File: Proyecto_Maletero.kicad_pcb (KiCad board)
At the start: 2 copper layers, 44 parts, among them J1 DE9_Pins, J2 Conn_01x02, J3 Conn_01x02, J4 Conn_01x03, J5 Conn_01x02, J6 DE9_Pins, J8 Conn_01x02, J9 Conn_01x02, K1 FINDER-34.51, Q2 MMBT5550L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

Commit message: Layout inicio
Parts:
- removed C17: 100n, Capacitor_SMD:C_0805_2012Metric
- J8, J9: footprint TerminalBlock_Phoenix:TerminalBlock_Phoenix_MKDS-1,5-3-5.08_1x03_P5.08mm_Horizontal -> TerminalBlock_Phoenix:TerminalBlock_Phoenix_MKDS-1,5-2_1x02_P5.00mm_Horizontal
- moved R7 76.9 mm to (131.0, 54.3), turned to -90 degrees
- moved R6 71.8 mm to (125.7, 50.0)
- moved C13 56.4 mm to (117.8, 54.0), turned to -90 degrees
- moved U2 53.6 mm to (123.9, 54.3)
- moved C14 49.9 mm to (115.0, 70.4), turned to 90 degrees
- moved J6 47.2 mm to (128.6, 35.0), turned to -90 degrees
- moved C8 45.9 mm to (105.5, 38.6), turned to 180 degrees
- moved C18 43.0 mm to (80.2, 24.8), turned to 180 degrees
- moved C15 42.8 mm to (96.2, 25.0)
- moved C3 41.7 mm to (100.6, 56.6)
- moved R2 41.1 mm to (95.0, 49.5), turned to -90 degrees
- moved C4 40.5 mm to (95.5, 45.5), turned to -90 degrees
- moved K1 39.3 mm to (106.5, 42.2)
- moved C5 38.4 mm to (91.5, 45.5), turned to -90 degrees
- moved R1 37.9 mm to (92.2, 49.4), turned to 90 degrees
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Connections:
- C7 pad 1: Osc_1 -> Osc_2
- C9 pad 1: GND -> VRth
- C9 pad 2: VCC -> GND
- J3 pad 1: VBAT -> VBATERIA
- U7 pad 5: unconnected-(U7-VM-Pad5) -> VBAT
- Y1 pad 1: Osc_1 -> Osc_2
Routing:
- net VCC: track 0.00 -> 138.6 mm
- net VBAT: track 0.00 -> 51.4 mm
- net GND: track 0.00 -> 18.1 mm, vias 0 -> 21
- net SENSE: track 0.00 -> 16.2 mm
- net VBATERIA: track 0.00 -> 13.3 mm
- net Net-(D2-A): track 0.00 -> 10.2 mm
- net VRth: track 0.00 -> 6.35 mm
- net Net-(Q2-B): track 0.00 -> 5.67 mm
- net Vopam: track 0.00 -> 5.37 mm
- added copper zone on B.Cu, net GND

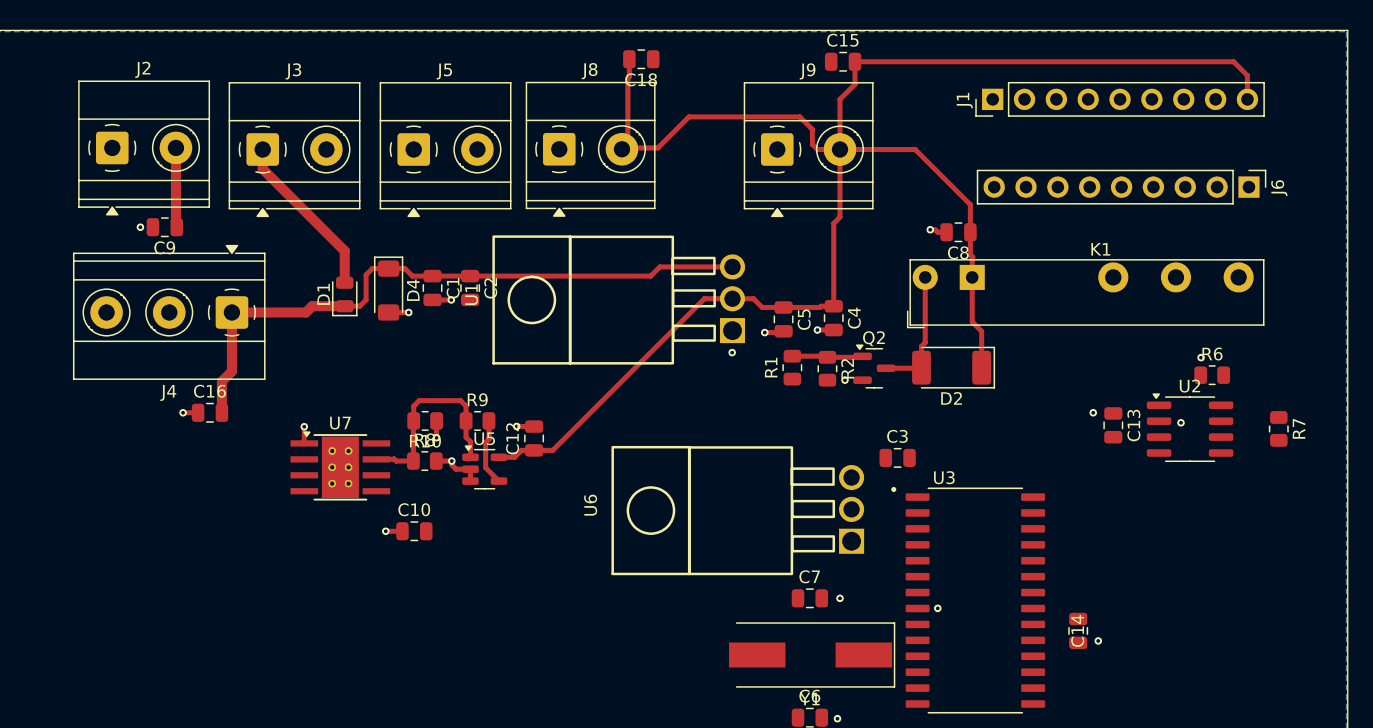
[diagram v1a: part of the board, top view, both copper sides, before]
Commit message: Capas y DE-9
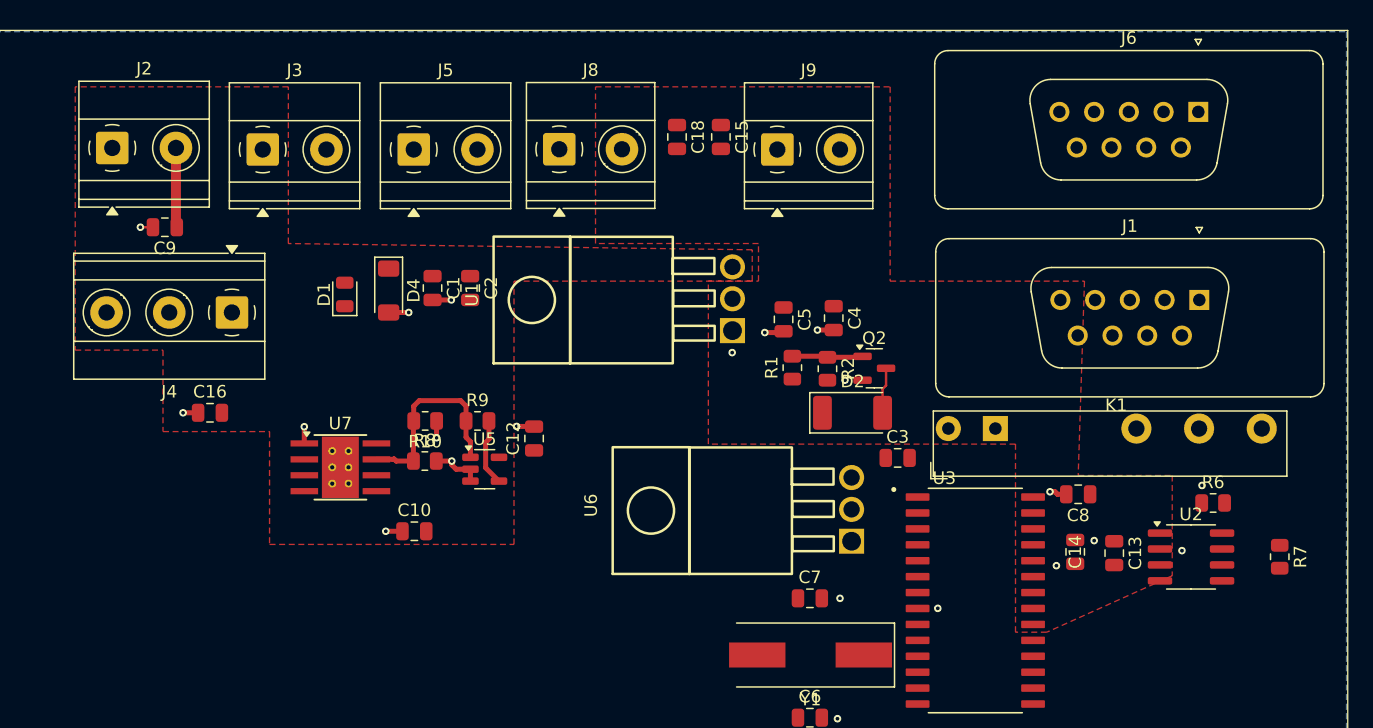
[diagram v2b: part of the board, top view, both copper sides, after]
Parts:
- J1, J6: footprint Connector_PinHeader_2.54mm:PinHeader_1x09_P2.54mm_Vertical -> Connector_Dsub:DSUB-9_Socket_Vertical_P2.77x2.84mm
- moved C8 23.0 mm to (115.0, 59.5)
- moved J1 23.0 mm to (124.7, 44.0), turned to 0 degrees
- moved K1 12.2 mm to (108.4, 54.3)
- moved C15 11.4 mm to (86.5, 31.0), turned to -90 degrees
- moved R6 10.2 mm to (125.8, 60.2)
- moved R7 10.2 mm to (131.1, 64.5)
- moved U2 10.2 mm to (124.0, 64.5)
- moved C13 10.2 mm to (117.9, 64.2)
- moved D2 8.68 mm to (97.0, 53.0), turned to 0 degrees
- moved J6 7.23 mm to (124.6, 29.0), turned to 0 degrees
- moved C18 6.82 mm to (83.0, 31.0), turned to -90 degrees
- moved C14 6.31 mm to (114.8, 64.1)
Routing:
- net VCC: track 138.6 -> 0.00 mm
- net VBAT: track 51.4 -> 0.00 mm
- net VBATERIA: track 13.3 -> 0.00 mm
- net Net-(D2-A): track 10.2 -> 3.66 mm
- net GND: track 18.1 -> 19.1 mm
- added copper zone on F.Cu, net VBAT
- added copper zone on F.Cu, net VCC

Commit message: Actulizacion layout
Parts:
- J1, J6: footprint Connector_Dsub:DSUB-9_Socket_Vertical_P2.77x2.84mm -> Connector_Dsub:DSUB-9_Pins_Horizontal_P2.77x2.84mm_EdgePinOffset4.94mm_Housed_MountingHolesOffset4.94mm
- moved J6 97.6 mm to (38.0, 74.1)
- moved C8 78.5 mm to (36.5, 59.2), turned to -90 degrees
- moved K1 78.1 mm to (30.5, 60.2), turned to 90 degrees
- moved R7 53.0 mm to (78.4, 59.4), turned to 0 degrees
- moved D2 47.3 mm to (49.7, 53.0), turned to -90 degrees
- moved Q2 45.8 mm to (53.2, 54.7), turned to -90 degrees
- moved C3 44.7 mm to (56.0, 54.4), turned to 90 degrees
- moved R6 43.1 mm to (82.7, 63.1)
- moved U2 42.9 mm to (81.2, 67.2)
- moved C6 42.5 mm to (54.4, 61.0), turned to 180 degrees
- moved R2 41.8 mm to (53.2, 51.0), turned to 180 degrees
- moved J1 41.2 mm to (94.1, 71.6), turned to 90 degrees
- moved Y1 39.8 mm to (54.3, 66.0), turned to 0 degrees
- moved C14 39.4 mm to (76.4, 73.2)
- moved C7 39.3 mm to (54.4, 70.5), turned to 180 degrees
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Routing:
- net Sensor_Pie: track 0.00 -> 16.4 mm
- net VCC: track 0.00 -> 14.1 mm
- net VRth: track 6.35 -> 0.09 mm
- net GND: track 19.1 -> 24.5 mm, vias 21 -> 19
- net Net-(D2-A): track 3.66 -> 0.00 mm
- net VBAT: track 0.00 -> 2.76 mm
- removed copper zone on F.Cu, net VBAT
- removed copper zone on F.Cu, net VCC
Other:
- board outline added: 74.8 x 59.6 mm

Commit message: Layout final v.1
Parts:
- added REF**: MountingHole_2.5mm, MountingHole:MountingHole_2.5mm, F.Cu at (95.8, 76.8)
- added REF**: MountingHole_2.5mm, MountingHole:MountingHole_2.5mm, F.Cu at (29.9, 28.6)
- added REF**: MountingHole_2.5mm, MountingHole:MountingHole_2.5mm, F.Cu at (31.6, 78.1)
- added REF**: MountingHole_2.5mm, MountingHole:MountingHole_2.5mm, F.Cu at (98.8, 27.4)
- J1, J6: footprint Connector_Dsub:DSUB-9_Pins_Horizontal_P2.77x2.84mm_EdgePinOffset4.94mm_Housed_MountingHolesOffset4.94mm -> Connector_Dsub:DSUB-9_Pins_Horizontal_P2.77x2.54mm_EdgePinOffset9.40mm
- moved J6 38.3 mm to (76.1, 70.0)
- moved C3 35.9 mm to (36.8, 24.1), turned to 0 degrees
- moved C6 17.0 mm to (38.5, 67.0)
- moved C7 16.8 mm to (38.3, 75.4)
- moved C9 13.4 mm to (64.9, 23.8), turned to 0 degrees
- moved C14 13.4 mm to (63.4, 69.8)
- moved U3 12.6 mm to (55.6, 68.9)
- moved Y1 11.9 mm to (43.5, 70.8), turned to 90 degrees
- moved C16 8.45 mm to (50.9, 37.3), turned to 180 degrees
- moved R1 7.84 mm to (49.7, 55.2), turned to 180 degrees
- moved D2 6.65 mm to (55.8, 50.3), turned to 90 degrees
- moved Q2 6.33 mm to (49.7, 49.5), turned to 90 degrees
- moved R7 6.26 mm to (82.5, 64.1), turned to -90 degrees
- moved C13 5.51 mm to (77.2, 67.3)
- moved U2 5.51 mm to (77.3, 63.3)
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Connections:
- C1 pad 2: GND -> GNDPWR
- C10 pad 1: GND -> GNDPWR
- C12 pad 2: GND -> GNDPWR
- C15 pad 1: GND -> GNDPWR
- C16 pad 1: GND -> GNDPWR
- C18 pad 1: GND -> GNDPWR
- C2 pad 2: GND -> GNDPWR
- C3 pad 2: GND -> GNDPWR
- C4 pad 2: GND -> GNDPWR
- C5 pad 2: GND -> GNDPWR
- C8 pad 2: GND -> GNDPWR
- C9 pad 2: GND -> GNDPWR
- D4 pad 2: GND -> GNDPWR
- J2 pad 1: GND -> GNDPWR
- J3 pad 2: GND -> GNDPWR
- J4 pad 2: GND -> GNDPWR
- Q2 pad 2: GND -> GNDPWR
- R10 pad 1: GND -> GNDPWR
- R2 pad 2: GND -> GNDPWR
- R8 pad 2: GND -> GNDPWR
- U1 pad 1: GND -> GNDPWR
- U5 pad 2: GND -> GNDPWR
- U5 pad 3: GND -> GNDPWR
- U6 pad 1: GND -> unconnected-(U6-GND-Pad1)
- U7 pad 1: GND -> GNDPWR
- U7 pad 9: GND -> GNDPWR
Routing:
- net VCC: track 14.1 -> 180.6 mm, vias 0 -> 1
- net VBAT: track 2.76 -> 97.4 mm, vias 0 -> 2
- net SENAL_RELE: track 0.00 -> 65.8 mm
- net Manual_Close: track 0.00 -> 64.6 mm, vias 0 -> 2
- net Sensor_Pie: track 16.4 -> 75.6 mm
- net VRth: track 0.09 -> 53.8 mm
- net Vopam: track 5.37 -> 41.0 mm, vias 0 -> 2
- net Net-(D2-A): track 0.00 -> 34.1 mm
- net Motor+: track 0.00 -> 28.9 mm, vias 0 -> 2
- net Motor-: track 0.00 -> 28.2 mm, vias 0 -> 2
- net PH_B: track 0.00 -> 25.4 mm
- net INPUT_RELE: track 0.00 -> 25.1 mm
- net GNDPWR: track 0.00 -> 24.9 mm, vias 0 -> 19
- net TX_USART: track 0.00 -> 23.8 mm
- net CAN_TX: track 0.00 -> 22.3 mm
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- added copper zone on B.Cu, net GNDPWR
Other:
- board size 74.8 x 59.6 mm -> 75.2 x 59.5 mm

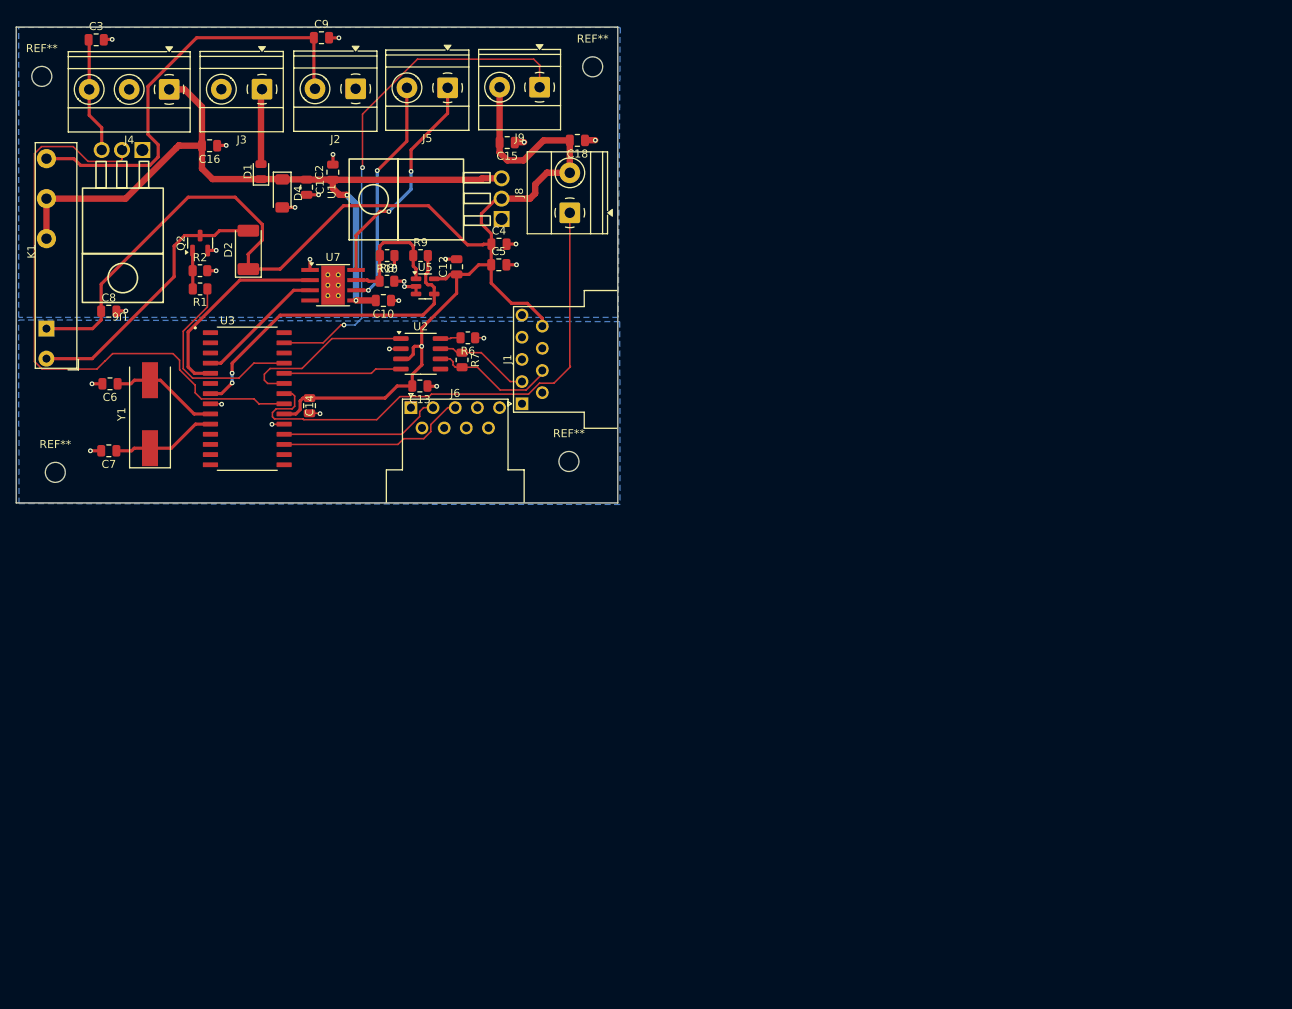
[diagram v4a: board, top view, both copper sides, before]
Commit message: Actualizaciones y primeros pasos para correfir errores
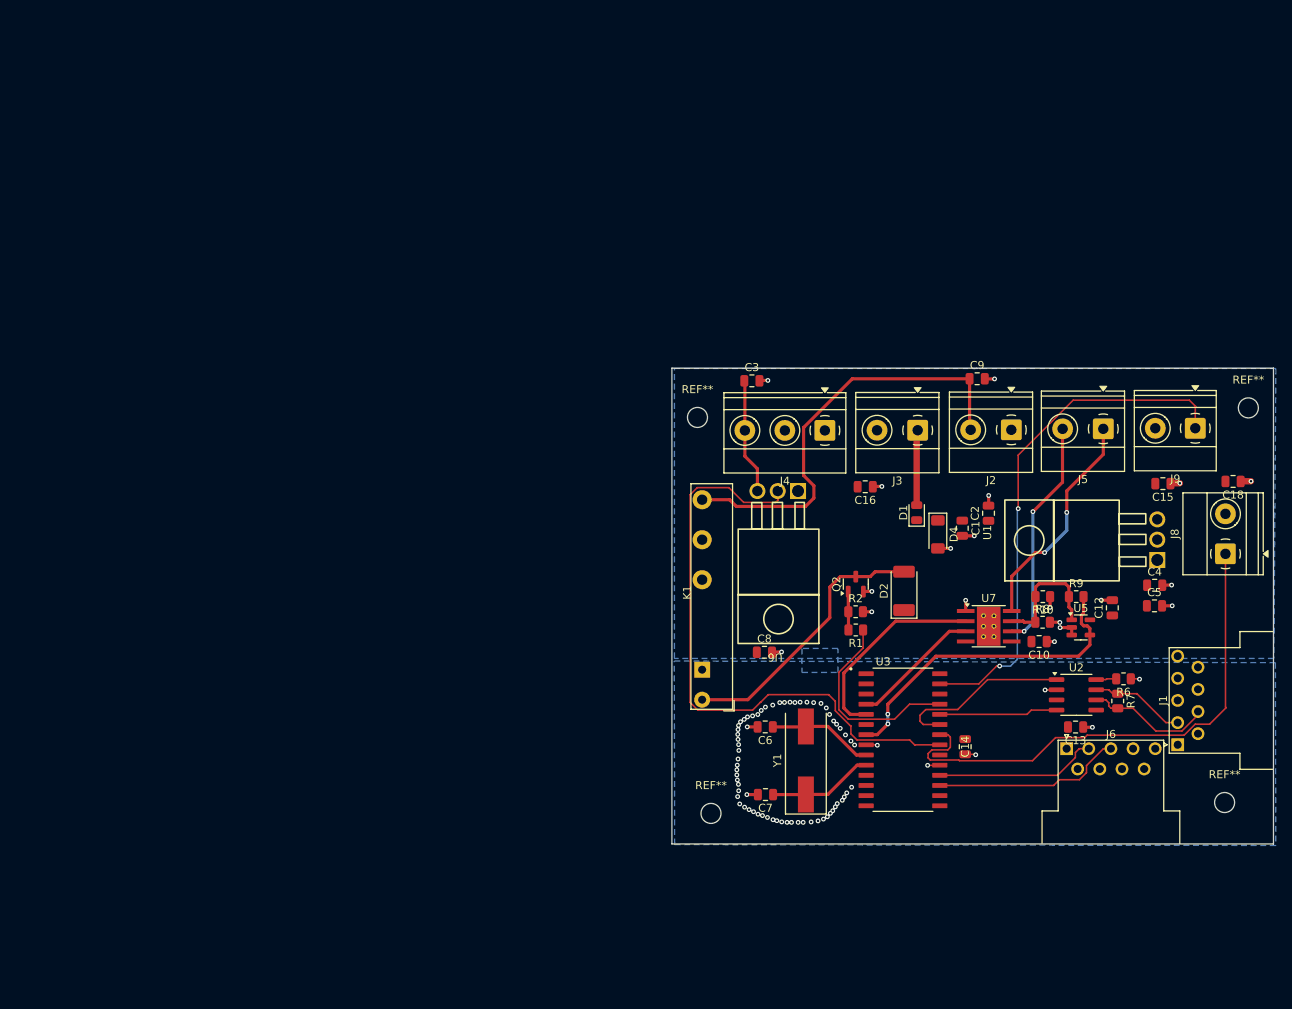
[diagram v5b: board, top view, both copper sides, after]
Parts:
- moved Y1 92.7 mm to (125.5, 114.1)
- moved C7 92.7 mm to (120.4, 118.4)
- moved C6 92.5 mm to (120.4, 109.9)
- moved C10 92.4 mm to (154.6, 99.3)
- moved C14 92.4 mm to (145.4, 112.4)
- moved C15 92.4 mm to (170.1, 79.5)
- moved C18 92.4 mm to (178.9, 79.3)
- moved C4 92.4 mm to (169.1, 92.2)
- moved C8 92.4 mm to (120.3, 100.6)
- moved C9 92.4 mm to (146.9, 66.4)
- moved D1 92.4 mm to (139.3, 83.2)
- moved D4 92.4 mm to (142.0, 85.9)
- moved J1 92.4 mm to (171.9, 112.2)
- moved J3 92.4 mm to (139.4, 72.9)
- moved J6 92.4 mm to (158.1, 112.7)
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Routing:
- net VCC: track 180.6 -> 0.00 mm, vias 1 -> 0
- net VBAT: track 97.4 -> 0.00 mm, vias 2 -> 0
- net GND: track 10.7 -> 10.8 mm, vias 8 -> 72
